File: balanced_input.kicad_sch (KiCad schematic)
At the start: 24 parts, among them J1 XLR3_Ground

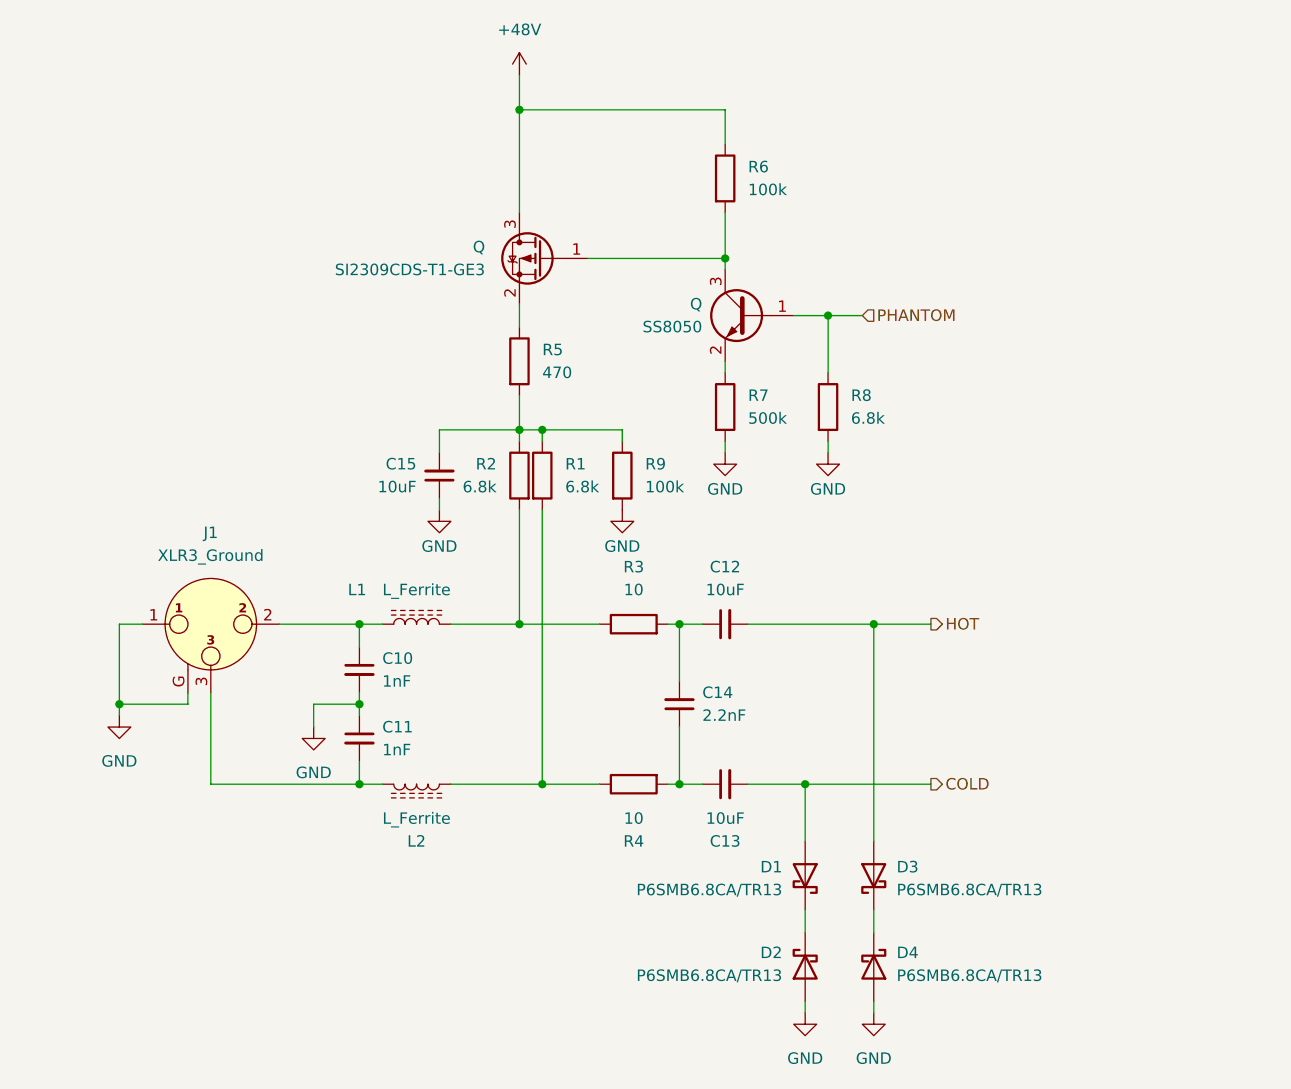
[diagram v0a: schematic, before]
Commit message: some suggested changes to the schematic:
- common pull-down mosfet for phantom power switch
- added board interconnect header
- proposed buffer for VREF
- cosmetic changes
- address selection jumpers
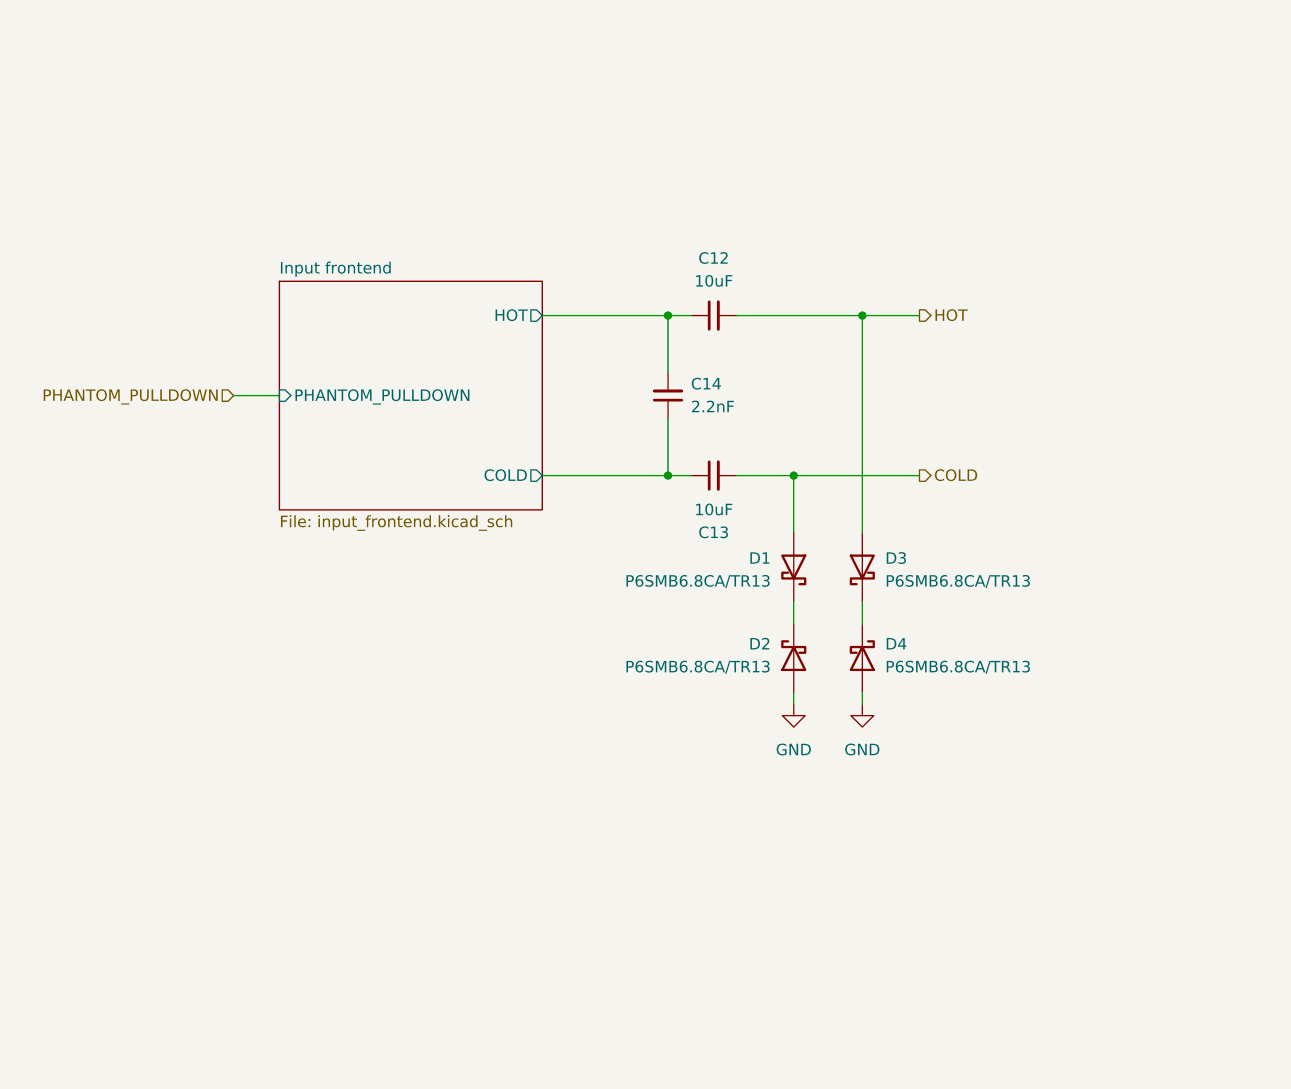
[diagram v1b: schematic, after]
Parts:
- removed C10, C11: 1nF, Capacitor_SMD:C_0603_1608Metric, symbol Device:C_Small
- removed C15: 10uF, Capacitor_SMD:C_0603_1608Metric, symbol Device:C_Small
- removed J1: XLR3_Ground, symbol Connector_Audio:XLR3_Ground
- removed L1, L2: L_Ferrite, symbol Device:L_Ferrite
- removed Q: SS8050, Package_TO_SOT_SMD:SOT-23, symbol Transistor_BJT:SS8050
- removed Q: SI2309CDS-T1-GE3, Package_TO_SOT_SMD:SOT-23, symbol Transistor_FET:Si2371EDS
- removed R1, R2, R8: 6.8k, Resistor_SMD:R_0603_1608Metric, symbol Device:R
- removed R3, R4: 10, Resistor_SMD:R_0603_1608Metric, symbol Device:R
- removed R5: 470, Resistor_SMD:R_0603_1608Metric, symbol Device:R
- removed R6, R9: 100k, Resistor_SMD:R_0603_1608Metric, symbol Device:R
- removed R7: 500k, Resistor_SMD:R_0603_1608Metric, symbol Device:R
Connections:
- net Input frontend/COLD: now reaches C13.1, C14.1
- net Input frontend/HOT: now reaches C12.1, C14.2
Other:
- added sheet Input frontend (input_frontend.kicad_sch)
- moved on the sheet: C12, C13, C14, D1, D2, D3, D4

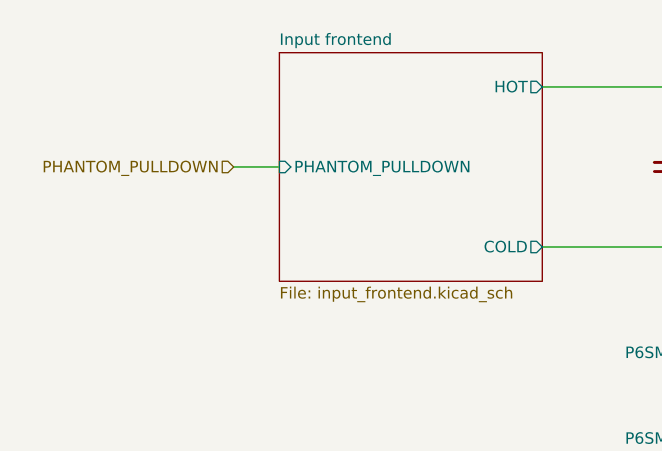
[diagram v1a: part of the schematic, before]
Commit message: independent phantom control and removed transformer bias
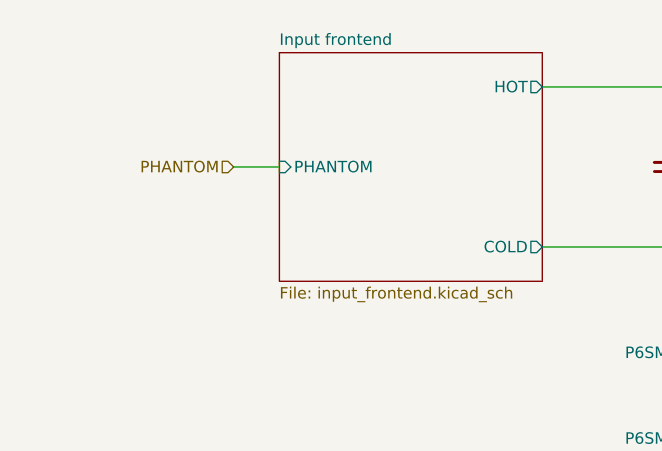
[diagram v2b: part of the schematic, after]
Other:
- sheet Input frontend ports: added PHANTOM; removed PHANTOM_PULLDOWN
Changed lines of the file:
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@@
-		)
-	)
-	(hierarchical_label "PHANTOM_PULLDOWN"
-		(shape input)
-		(at 97.79 78.74 180)
-		(effects
-			(font
-				(size 1.27 1.27)
-			)
-			(justify right)
 		)
 	)
@@
 		)
 	)
+	(hierarchical_label "PHANTOM"
+		(shape input)
+		(at 97.79 78.74 180)
+		(effects
+			(font
+				(size 1.27 1.27)
+			)
+			(justify right)
+		)
+	)
 	(hierarchical_label "HOT"
 		(shape output)
@@
 			)
 		)
-		(pin "PHANTOM_PULLDOWN" input
+		(pin "PHANTOM" input
 			(at 102.87 78.74 180)
 			(effects

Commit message: assign some component data
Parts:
- C10: renamed from C14; value 2.2nF -> 2.2nF 63V; MPN (none) -> C 2.2nF 63V 0805
- C11: renamed from C12; value 10uF -> 10uF 63V; MPN (none) -> C 10μF 63V 0805
- C12: renamed from C13; value 10uF -> 10uF 63V; MPN (none) -> C 10μF 63V 0805
- D1, D2, D3, D4: MPN (none) -> P6SMB6.8CA/TR13
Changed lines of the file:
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@@
+			)
+		)
+		(property "MPN" "P6SMB6.8CA/TR13"
+			(at 167.64 97.79 90)
+			(effects
+				(font
+					(size 1.27 1.27)
+				)
+				(hide yes)
 			)
 		)
@@
 		)
 		(property "LCSC" "C78395"
+			(at 167.64 107.95 90)
+			(effects
+				(font
+					(size 1.27 1.27)
+				)
+				(hide yes)
+			)
+		)
+		(property "MPN" "P6SMB6.8CA/TR13"
 			(at 167.64 107.95 90)
 			(effects
@@
 			)
 		)
+		(property "MPN" "P6SMB6.8CA/TR13"
+			(at 160.02 107.95 90)
+			(effects
+				(font
+					(size 1.27 1.27)
+				)
+				(hide yes)
+			)
+		)
 		(pin "1"
 		)
@@
 		(dnp no)
 		(fields_autoplaced yes)
-		(property "Reference" "#PWR019"
+		(property "Reference" "#PWR036"
 			(at 167.64 119.38 0)
 			(effects
@@
 			(project "mv2_taa3040"
 				(path "/41a55a1d-5108-482f-b313-9eaa5d011dff/e3f94415-cffd-4131-bc0e-4234c6300c0c"
-					(reference "#PWR019")
-					(unit 1)
-				)
-				(path "/41a55a1d-5108-482f-b313-9eaa5d011dff/ec88f180-6d4b-439f-8697-a1ff92f435a7"
-					(reference "#PWR033")
+					(reference "#PWR036")
+					(unit 1)
+				)
+				(path "/41a55a1d-5108-482f-b313-9eaa5d011dff/ec88f180-6d4b-439f-8697-a1ff92f435a7"
+					(reference "#PWR038")
 					(unit 1)
 				)
@@
 		(on_board yes)
 		(dnp no)
-		(property "Reference" "C13"
+		(property "Reference" "C12"
 			(at 151.1363 93.98 90)
 			(effects
@@
 			)
 		)
-		(property "Value" "10uF"
+		(property "Value" "10uF 63V"
 			(at 151.1363 91.44 90)
 			(effects
@@
 			)
 		)
+		(property "MPN" "C 10μF 63V 0805"
+			(at 151.13 87.63 90)
+			(effects
+				(font
+					(size 1.27 1.27)
+				)
+				(hide yes)
+			)
+		)
 		(pin "1"
 		)
@@
 			(project "mv2_taa3040"
 				(path "/41a55a1d-5108-482f-b313-9eaa5d011dff/e3f94415-cffd-4131-bc0e-4234c6300c0c"
-					(reference "C13")
-					(unit 1)
-				)
-				(path "/41a55a1d-5108-482f-b313-9eaa5d011dff/ec88f180-6d4b-439f-8697-a1ff92f435a7"
-					(reference "C21")
+					(reference "C12")
+					(unit 1)
+				)
+				(path "/41a55a1d-5108-482f-b313-9eaa5d011dff/ec88f180-6d4b-439f-8697-a1ff92f435a7"
+					(reference "C15")
 					(unit 1)
 				)
@@
 		(on_board yes)
 		(dnp no)
-		(property "Reference" "C14"
+		(property "Reference" "C10"
 			(at 148.59 77.4635 0)
 			(effects
@@
 			)
 		)
-		(property "Value" "2.2nF"
+		(property "Value" "2.2nF 63V"
 			(at 148.59 80.0035 0)
 			(effects
@@
 			)
 		)
+		(property "MPN" "C 2.2nF 63V 0805"
+			(at 146.05 78.74 0)
+			(effects
+				(font
+					(size 1.27 1.27)
+				)
+				(hide yes)
+			)
+		)
 		(pin "1"
 		)
@@
 			(project "mv2_taa3040"
 				(path "/41a55a1d-5108-482f-b313-9eaa5d011dff/e3f94415-cffd-4131-bc0e-4234c6300c0c"
-					(reference "C14")
-					(unit 1)
-				)
-				(path "/41a55a1d-5108-482f-b313-9eaa5d011dff/ec88f180-6d4b-439f-8697-a1ff92f435a7"
-					(reference "C19")
+					(reference "C10")
+					(unit 1)
+				)
+				(path "/41a55a1d-5108-482f-b313-9eaa5d011dff/ec88f180-6d4b-439f-8697-a1ff92f435a7"
+					(reference "C13")
 					(unit 1)
 				)
@@
 		(dnp no)
 		(fields_autoplaced yes)
-		(property "Reference" "C12"
+		(property "Reference" "C11"
 			(at 151.1363 63.5 90)
 			(effects
@@
 			)
 		)
-		(property "Value" "10uF"
+		(property "Value" "10uF 63V"
 			(at 151.1363 66.04 90)
 			(effects
@@
 			)
 		)
+		(property "MPN" "C 10μF 63V 0805"
+			(at 151.13 69.85 90)
+			(effects
+				(font
+					(size 1.27 1.27)
+				)
+				(hide yes)
+			)
+		)
 		(pin "1"
 		)
@@
 			(project "mv2_taa3040"
 				(path "/41a55a1d-5108-482f-b313-9eaa5d011dff/e3f94415-cffd-4131-bc0e-4234c6300c0c"
-					(reference "C12")
-					(unit 1)
-				)
-				(path "/41a55a1d-5108-482f-b313-9eaa5d011dff/ec88f180-6d4b-439f-8697-a1ff92f435a7"
-					(reference "C20")
+					(reference "C11")
+					(unit 1)
+				)
+				(path "/41a55a1d-5108-482f-b313-9eaa5d011dff/ec88f180-6d4b-439f-8697-a1ff92f435a7"
+					(reference "C14")
 					(unit 1)
 				)
@@
 		(dnp no)
 		(fields_autoplaced yes)
-		(property "Reference" "#PWR018"
+		(property "Reference" "#PWR035"
 			(at 160.02 119.38 0)
 			(effects
@@
 			(project "mv2_taa3040"
 				(path "/41a55a1d-5108-482f-b313-9eaa5d011dff/e3f94415-cffd-4131-bc0e-4234c6300c0c"
-					(reference "#PWR018")
-					(unit 1)
-				)
-				(path "/41a55a1d-5108-482f-b313-9eaa5d011dff/ec88f180-6d4b-439f-8697-a1ff92f435a7"
-					(reference "#PWR031")
+					(reference "#PWR035")
+					(unit 1)
+				)
+				(path "/41a55a1d-5108-482f-b313-9eaa5d011dff/ec88f180-6d4b-439f-8697-a1ff92f435a7"
+					(reference "#PWR037")
 					(unit 1)
 				)
@@
 			(at 160.02 97.79 90)
 			(effects
+				(font
+					(size 1.27 1.27)
+				)
+				(hide yes)
+			)
+		)
+		(property "MPN" "P6SMB6.8CA/TR13"
+			(at 160.02 97.79 90)
+			(effects

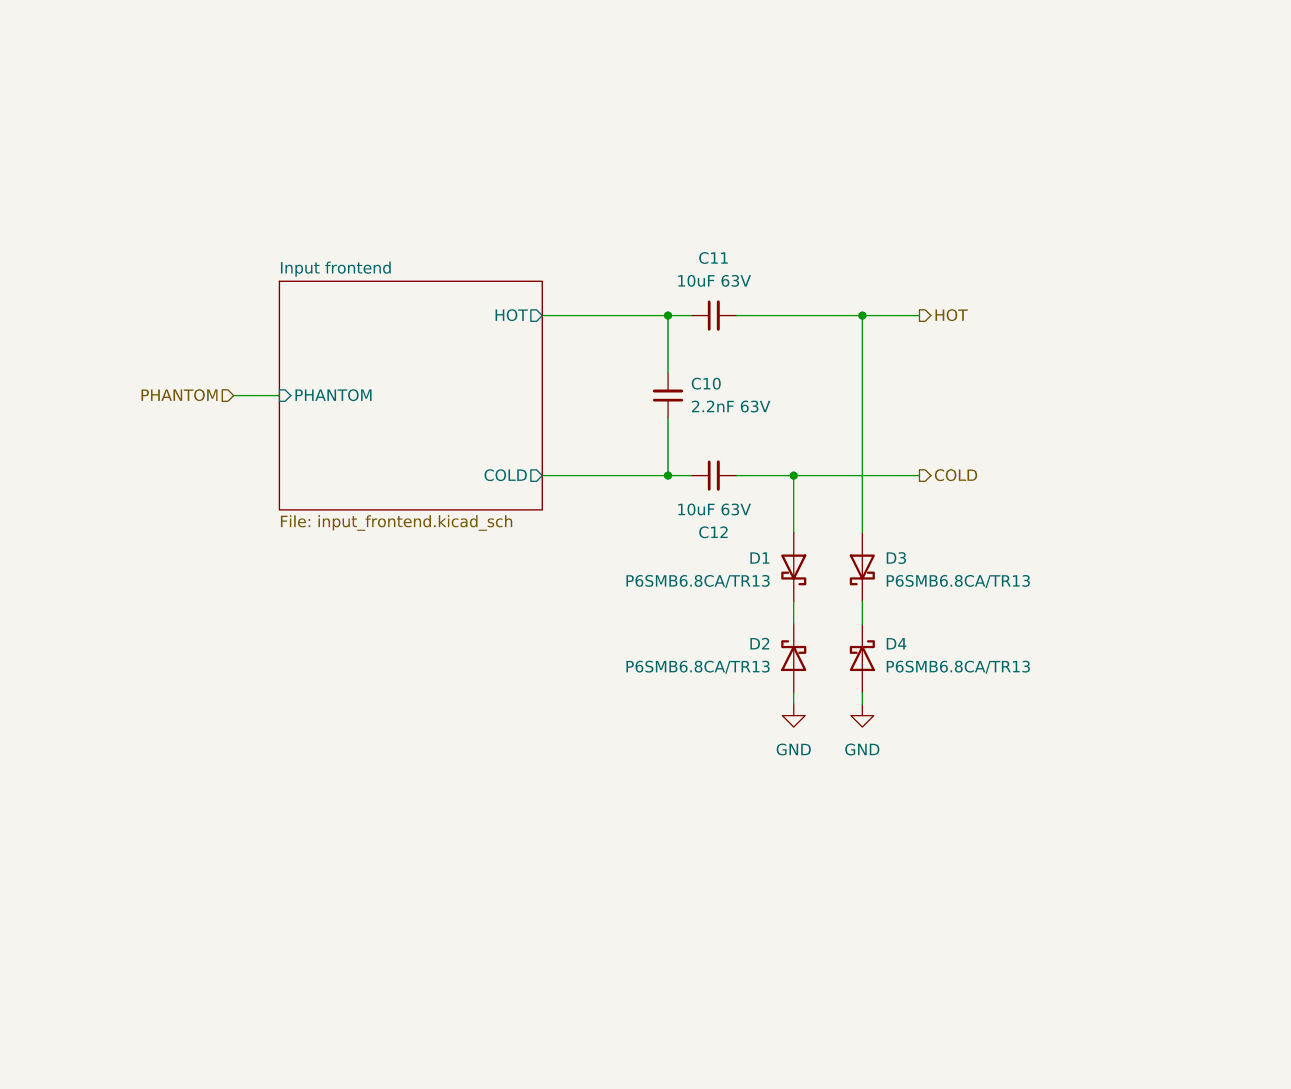
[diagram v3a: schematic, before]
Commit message: tvs clamps
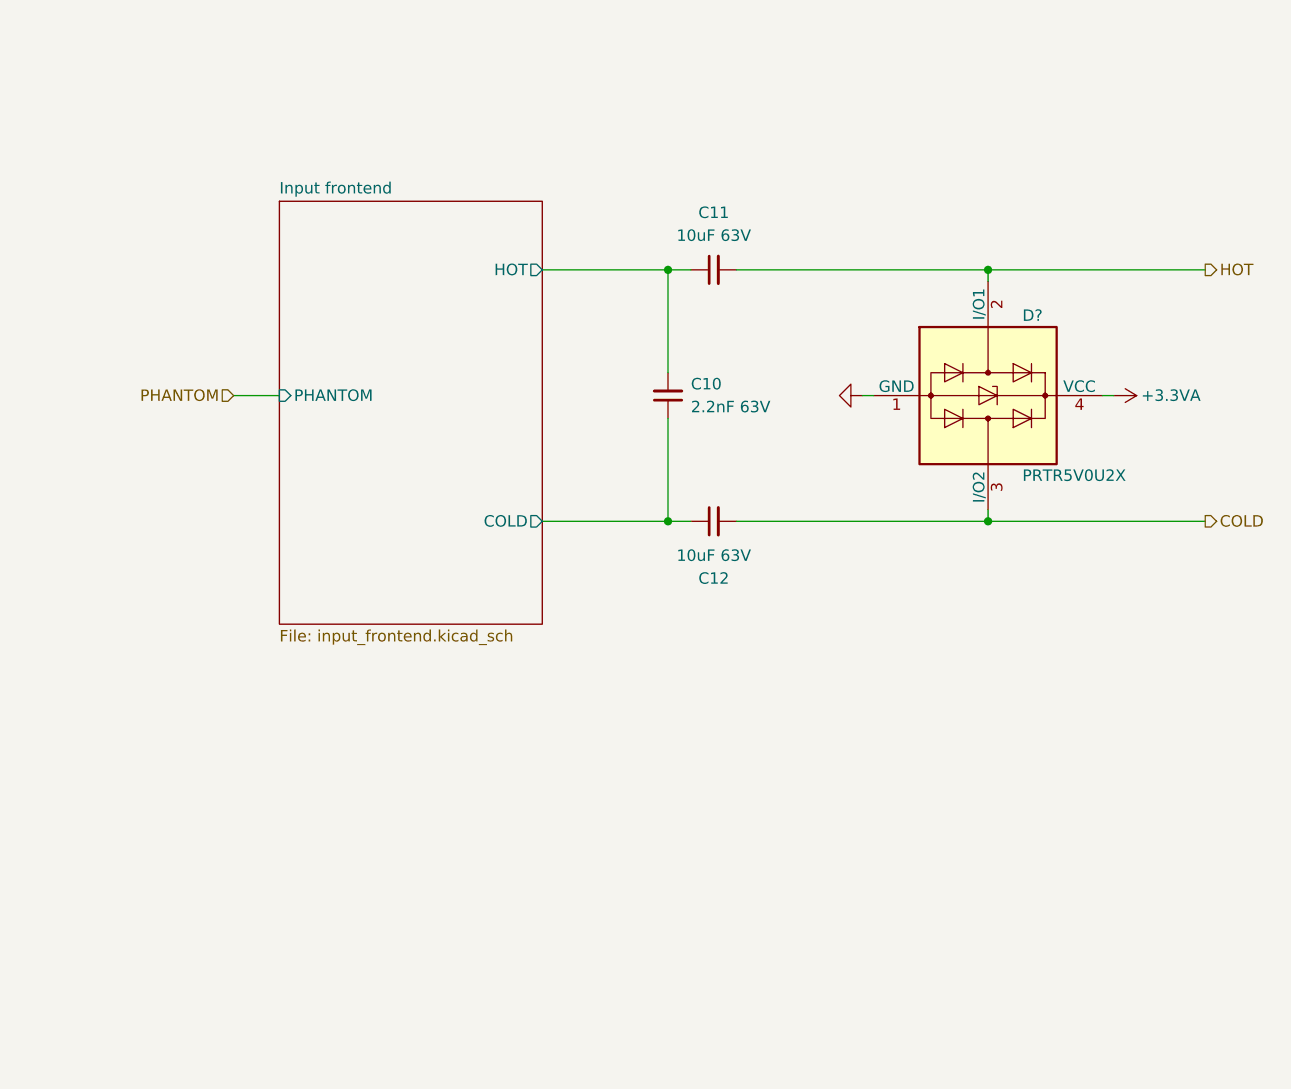
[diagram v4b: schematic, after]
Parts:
- removed D1, D2, D3, D4: P6SMB6.8CA/TR13, Diode_SMD:D_SMB, symbol Device:D_Schottky
- added D?: PRTR5V0U2X, Package_TO_SOT_SMD:SOT-143, symbol Power_Protection:PRTR5V0U2X
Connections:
- net COLD: now also D?.3 (I/O2)
- net GND: now also D?.1 (GND)
- net HOT: now also D?.2 (I/O1)
- new net +3.3VA: D?.4 (VCC)
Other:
- moved on the sheet: C11, C12

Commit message: some final touches
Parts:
- gave numbers to parts that had none: 1
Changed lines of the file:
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@@
 		(on_board yes)
 		(dnp no)
-		(property "Reference" "D?"
+		(property "Reference" "D1"
 			(at 185.42 69.85 90)
 			(effects
@@
 			(project "mv2_taa3040"
 				(path "/41a55a1d-5108-482f-b313-9eaa5d011dff/e3f94415-cffd-4131-bc0e-4234c6300c0c"
-					(reference "D?")
+					(reference "D1")
 					(unit 1)
 				)
 				(path "/41a55a1d-5108-482f-b313-9eaa5d011dff/ec88f180-6d4b-439f-8697-a1ff92f435a7"
-					(reference "D?")
+					(reference "D2")
 					(unit 1)
 				)
@@
 		(dnp no)
 		(fields_autoplaced yes)
-		(property "Reference" "#PWR035"
+		(property "Reference" "#PWR026"
 			(at 161.29 78.74 0)
 			(effects
@@
 			(project ""
 				(path "/41a55a1d-5108-482f-b313-9eaa5d011dff/e3f94415-cffd-4131-bc0e-4234c6300c0c"
-					(reference "#PWR035")
+					(reference "#PWR026")
 					(unit 1)
 				)
 				(path "/41a55a1d-5108-482f-b313-9eaa5d011dff/ec88f180-6d4b-439f-8697-a1ff92f435a7"
-					(reference "#PWR036")
+					(reference "#PWR028")
 					(unit 1)
 				)
@@
 		(on_board yes)
 		(dnp no)
-		(property "Reference" "#PWR037"
+		(property "Reference" "#PWR027"
 			(at 191.77 78.74 0)
 			(effects
@@
 			(project "mv2_taa3040"
 				(path "/41a55a1d-5108-482f-b313-9eaa5d011dff/e3f94415-cffd-4131-bc0e-4234c6300c0c"
-					(reference "#PWR037")
+					(reference "#PWR027")
 					(unit 1)
 				)
 				(path "/41a55a1d-5108-482f-b313-9eaa5d011dff/ec88f180-6d4b-439f-8697-a1ff92f435a7"
-					(reference "#PWR038")
-					(unit 1)
-				)
+					(reference "#PWR029")
+					(unit 1)
+				)

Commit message: update component assignments
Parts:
- removed C12: 10uF 63V, Capacitor_SMD:C_0603_1608Metric, symbol Device:C_Small
- added C? (x2): 10μF 100V, Capacitor_THT:CP_Radial_D5.0mm_P2.00mm, symbol Device:C_Polarized
- added C?: 2.2uF 100V, Capacitor_SMD:C_1206_3216Metric, symbol Device:C_Small
- C10: MPN C 2.2nF 63V 0805 -> C 2.2nF 63V 0603
- C11: value 10uF 63V -> 2.2uF 100V; footprint Capacitor_SMD:C_0603_1608Metric -> Capacitor_SMD:C_1206_3216Metric; MPN C 10μF 63V 0805 -> C 2.2μF 100V 1206; now not fitted
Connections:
- net COLD: now also C?.2, C?.2
- net HOT: now also C?.2
- net Input frontend/COLD: now also C?.1, C?.1
- net Input frontend/HOT: now also C?.1
